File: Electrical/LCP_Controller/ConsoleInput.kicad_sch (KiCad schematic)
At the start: 4 parts, among them J31 SALEAE_TEST, J7 Conn_01x06

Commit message: Hardware Revision : v0.3
1. modified schematic design, removed unnecessary test points.
2. pcb layout 2x8 Inches allowance dimension, layout is in progress
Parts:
- renumbered C35 to C1, J7 to J2, J31 to J3, R23 to R1
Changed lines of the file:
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@@
   (symbol (lib_id "power:GND") (at 152.4 115.57 0) (unit 1)
     (in_bom yes) (on_board yes)
-    (property "Reference" "#PWR057" (id 0) (at 152.4 121.92 0)
+    (property "Reference" "#PWR02" (id 0) (at 152.4 121.92 0)
       (effects (font (size 1.27 1.27)) hide)
     )
@@
   (symbol (lib_id "Connector_Generic:Conn_02x04_Odd_Even") (at 176.53 127 0) (mirror y) (unit 1)
     (in_bom yes) (on_board yes)
-    (property "Reference" "J31" (id 0) (at 173.99 121.92 0)
+    (property "Reference" "J3" (id 0) (at 173.99 121.92 0)
       (effects (font (size 1.27 1.27)) (justify right))
     )
@@
   (symbol (lib_id "power:GND") (at 161.29 133.35 0) (unit 1)
     (in_bom yes) (on_board yes)
-    (property "Reference" "#PWR0119" (id 0) (at 161.29 139.7 0)
+    (property "Reference" "#PWR06" (id 0) (at 161.29 139.7 0)
       (effects (font (size 1.27 1.27)) hide)
     )
@@
   (symbol (lib_id "Connector_Generic:Conn_01x06") (at 124.46 92.71 0) (mirror y) (unit 1)
     (in_bom yes) (on_board yes)
-    (property "Reference" "J7" (id 0) (at 124.46 83.82 0))
+    (property "Reference" "J2" (id 0) (at 124.46 83.82 0))
     (property "Value" "Conn_01x06" (id 1) (at 124.46 104.14 0))
     (property "Footprint" "Connector_PinHeader_2.54mm:PinHeader_1x06_P2.54mm_Vertical" (id 2) (at 124.46 92.71 0)
@@
   (symbol (lib_id "Device:C") (at 143.51 102.87 270) (mirror x) (unit 1)
     (in_bom yes) (on_board yes)
-    (property "Reference" "C35" (id 0) (at 143.51 107.95 90))
+    (property "Reference" "C1" (id 0) (at 143.51 107.95 90))
     (property "Value" "0.1uF" (id 1) (at 143.51 110.49 90))
     (property "Footprint" "Capacitor_SMD:C_0805_2012Metric" (id 2) (at 139.7 101.9048 0)
@@
   (symbol (lib_id "Device:R") (at 152.4 109.22 0) (unit 1)
     (in_bom yes) (on_board yes)
-    (property "Reference" "R23" (id 0) (at 154.178 108.0516 0)
+    (property "Reference" "R1" (id 0) (at 154.178 108.0516 0)
       (effects (font (size 1.27 1.27)) (justify left))
     )
@@
   (symbol (lib_id "power:GND") (at 152.4 115.57 0) (unit 1)
     (in_bom yes) (on_board yes)
-    (property "Reference" "#PWR058" (id 0) (at 152.4 121.92 0)
+    (property "Reference" "#PWR03" (id 0) (at 152.4 121.92 0)
       (effects (font (size 1.27 1.27)) hide)
     )
@@
   (symbol (lib_id "power:GND") (at 152.4 115.57 0) (unit 1)
     (in_bom yes) (on_board yes)
-    (property "Reference" "#PWR059" (id 0) (at 152.4 121.92 0)
+    (property "Reference" "#PWR04" (id 0) (at 152.4 121.92 0)
       (effects (font (size 1.27 1.27)) hide)
     )
@@
   (symbol (lib_id "power:GND") (at 152.4 115.57 0) (unit 1)
     (in_bom yes) (on_board yes)
-    (property "Reference" "#PWR060" (id 0) (at 152.4 121.92 0)
+    (property "Reference" "#PWR05" (id 0) (at 152.4 121.92 0)
       (effects (font (size 1.27 1.27)) hide)
     )
@@
   (symbol (lib_id "power:GND") (at 156.21 86.36 0) (unit 1)
     (in_bom yes) (on_board yes)
-    (property "Reference" "#PWR061" (id 0) (at 156.21 92.71 0)
+    (property "Reference" "#PWR01" (id 0) (at 156.21 92.71 0)
       (effects (font (size 1.27 1.27)) hide)
     )

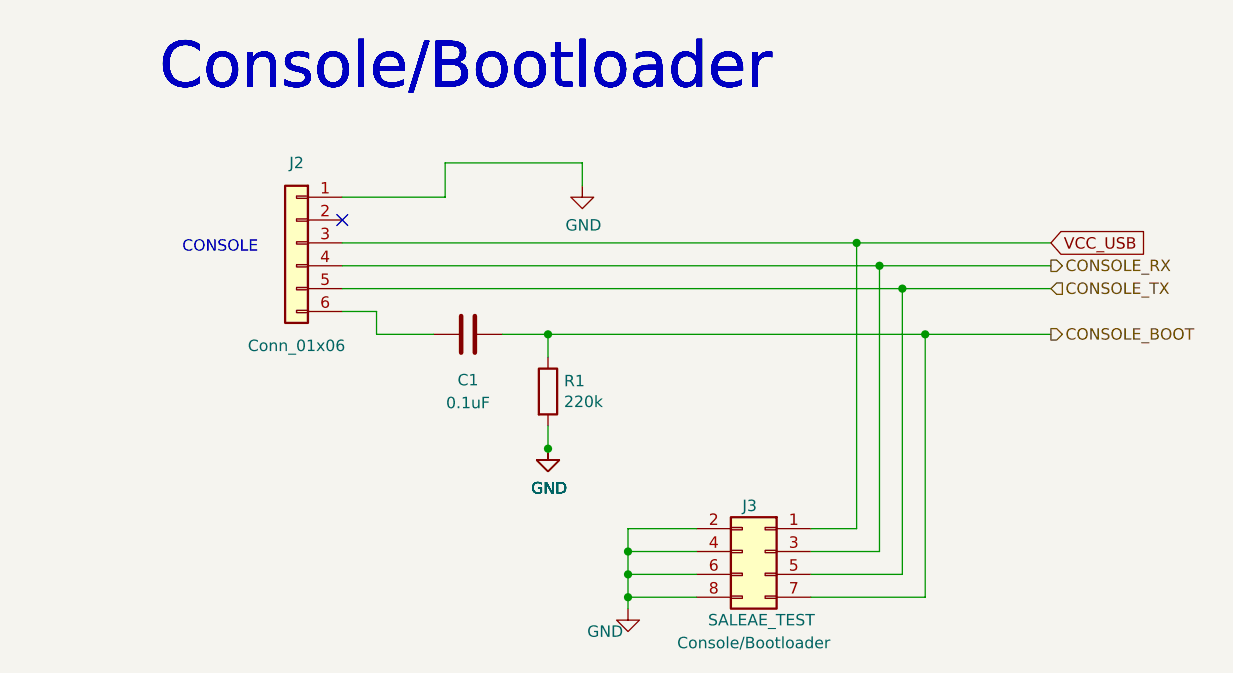
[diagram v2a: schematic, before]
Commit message: Connector Progress
J2 J22 and J23 converted to Molex Microfit

SALEAE TEST connectors removed
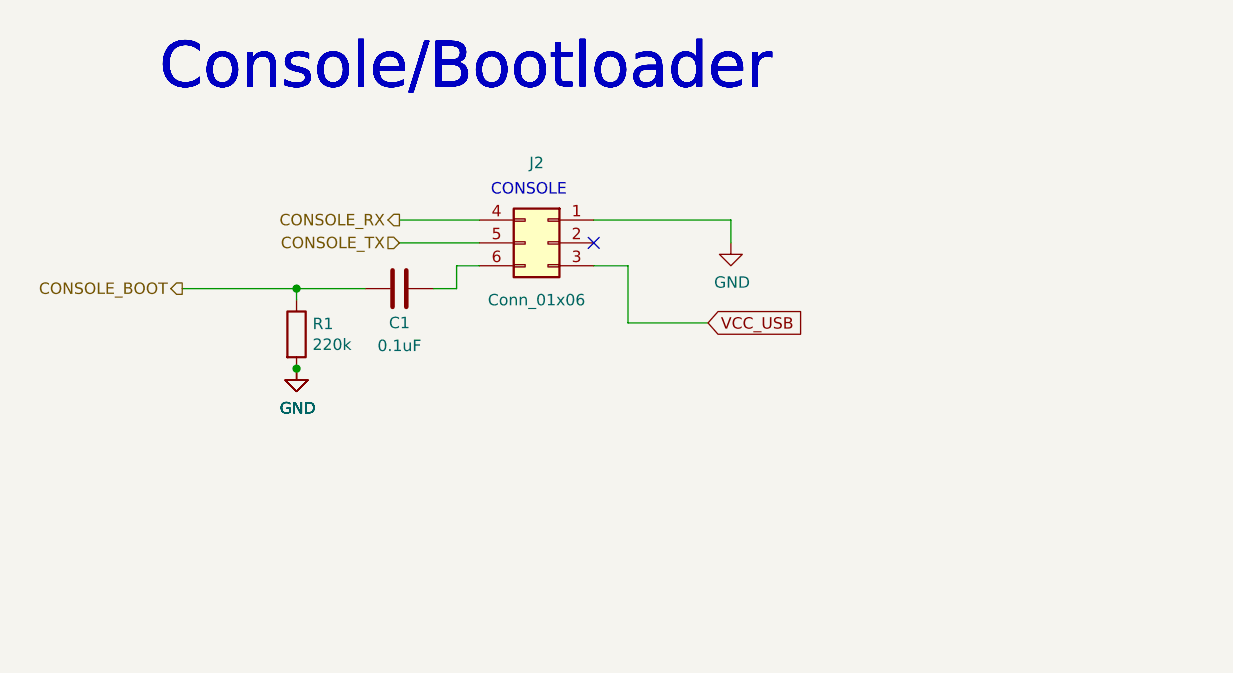
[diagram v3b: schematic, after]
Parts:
- removed J3: SALEAE_TEST, Connector_PinHeader_2.54mm:PinHeader_2x04_P2.54mm_Vertical, symbol Connector_Generic:Conn_02x04_Odd_Even
- J2: footprint Connector_PinHeader_2.54mm:PinHeader_1x06_P2.54mm_Vertical -> Connector_Molex:Molex_Micro-Fit_3.0_43045-0612_2x03_P3.00mm_Vertical; symbol Connector_Generic:Conn_01x06 -> Connector_Generic:Conn_02x03_Top_Bottom
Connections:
- net CONSOLE_BOOT: now also C1.2; no longer C1.1
- net at J2.6 (Pin_6): now also C1.1; no longer C1.2
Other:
- moved on the sheet: C1, J2, R1

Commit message: Board Revision 0.4
Completed
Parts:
- J2: MPN (none) -> 0430450612
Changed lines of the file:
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@@
   (title_block
     (title "LCP Controller ")
-    (date "2022-12-19")
-    (rev "0.3")
+    (date "2024-07-22")
+    (rev "0.4")
     (company "NOAA Pacific Marine Environmental Laboratory")
-    (comment 3 "Current design modified by: Basharat Basharat")
+    (comment 1 "https://github.com/PaulZC/Artemis_Global_Tracker")
+    (comment 2 "Based on Paul Clark's Sparkfun Artemis Global Tracker")
+    (comment 3 "Current Design Updated by: Joseph Kurina")
     (comment 4 "Current design by: Matt Casari")
     (comment 5 "Current design modified by: Basharat Martin")
+    (comment 6 "Current Design Updated by: Joseph Kurina")
   )
   (junction (at 124.46 97.79) (diameter 0) (color 0 0 0 0)
@@
       (effects (font (size 1.27 1.27)) hide)
     )
-    (property "MPN" "" (at 152.4 92.71 0)
+    (property "MPN" "0430450612" (at 152.4 92.71 0)
       (effects (font (size 1.27 1.27)) hide)
     )
